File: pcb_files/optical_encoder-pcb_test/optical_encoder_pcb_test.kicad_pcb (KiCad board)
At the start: 2 copper layers, 53.7 x 54.9 mm, 33 parts, among them J1 Conn_01x03_Pin, J2 Conn_01x05_Pin, J3 Conn_01x04_Pin, J4 Conn_01x04_Pin, J5 Conn_DF13_male_01x06, J6 Conn_DF13_male_01x05, J7 Conn_AMASS_male_01x03, J8 Conn_01x03_Pin, U1 AT24CS16-STUM, U2 AMS1117-3.3

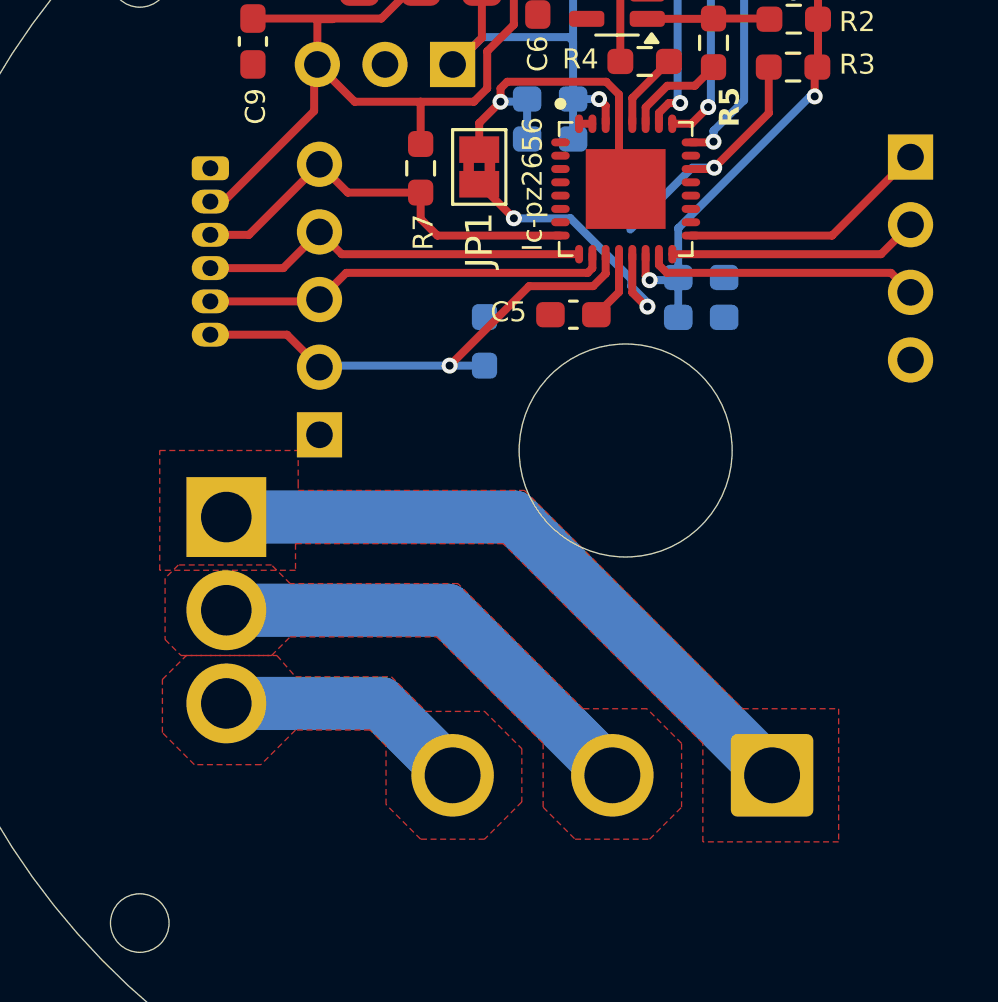
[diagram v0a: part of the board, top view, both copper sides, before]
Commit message: unconnected track removed
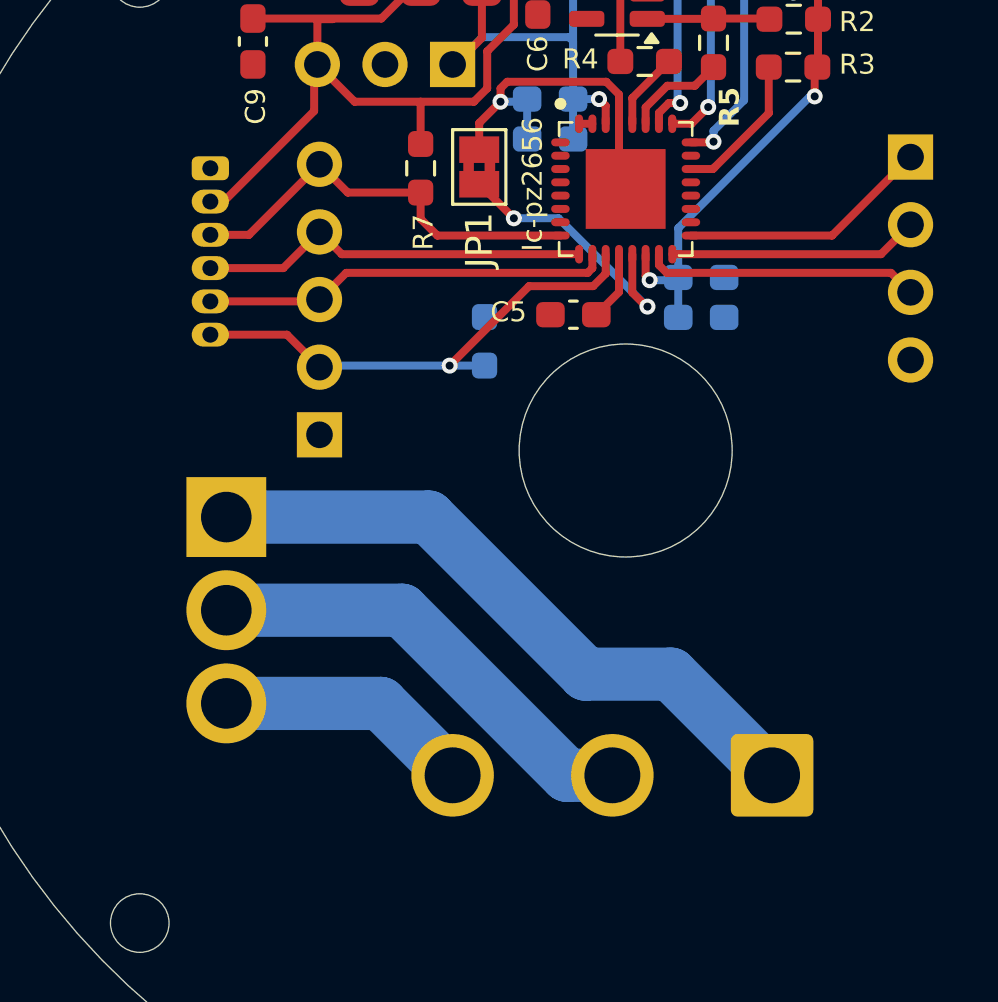
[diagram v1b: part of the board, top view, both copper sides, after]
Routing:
- net Net-(Ic-pz2656-NRES): track 9.64 -> 5.52 mm, vias 1 -> 0
- removed copper zone on F.Cu, net /P1
- removed copper zone on F.Cu, net /P2
- removed copper zone on F.Cu, net /P3
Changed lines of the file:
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@@
 			(pinfunction "Pin_1")
 			(pintype "passive")
+			(zone_connect 2)
+			(thermal_bridge_width 1)
+			(thermal_bridge_angle 45)
+			(thermal_gap 0.5)
 		)
 		(pad "2" thru_hole circle
@@
 	)
 	(gr_text "P1"
-		(at 124.7 133 -0)
+		(at 124.5 132.9 -0)
 		(layer "B.SilkS")
 		(effects
@@
 	)
 	(gr_text "P2"
-		(at 118.7 133 -0)
+		(at 118 134.1 -0)
 		(layer "B.SilkS")
 		(effects
@@
 	)
 	(gr_text "P3"
-		(at 112.7 133 -0)
+		(at 112.9 133.4 -0)
 		(layer "B.SilkS")
 		(effects
@@
 	)
 	(segment
-		(start 121.318804 116.941889)
+		(start 116.3 113.7775)
+		(end 117.9775 113.7775)
+		(width 0.3)
+		(layer "B.Cu")
+		(net 3)
+	)
+	(segment
+		(start 121.295871 117.095871)
 		(end 121.318804 117.095871)
 		(width 0.3)
@@
 	)
 	(segment
-		(start 120.713173 116.336258)
-		(end 121.318804 116.941889)
-		(width 0.3)
-		(layer "B.Cu")
-		(net 3)
-	)
-	(segment
-		(start 116.3 113.7775)
-		(end 118.427502 113.7775)
-		(width 0.3)
-		(layer "B.Cu")
-		(net 3)
-	)
-	(segment
-		(start 120.713173 116.063171)
-		(end 120.713173 116.336258)
-		(width 0.3)
-		(layer "B.Cu")
-		(net 3)
-	)
-	(segment
-		(start 118.427502 113.7775)
-		(end 120.713173 116.063171)
+		(start 117.9775 113.7775)
+		(end 121.295871 117.095871)
 		(width 0.3)
 		(layer "B.Cu")
@@
 		(net 17)
 	)
-	(via
-		(at 123.82644 111.87932)
-		(size 0.6)
-		(drill 0.3)
-		(layers "F.Cu" "B.Cu")
-		(net 17)
-	)
-	(segment
-		(start 122.99568 111.87932)
-		(end 120.675 114.2)
-		(width 0.3)
-		(layer "B.Cu")
-		(net 17)
-	)
-	(segment
-		(start 123.82644 111.87932)
-		(end 122.99568 111.87932)
-		(width 0.3)
-		(layer "B.Cu")
-		(net 17)
-	)
 	(segment
 		(start 107.64 115.65)
@@
 	)
 	(segment
-		(start 116.3 125)
+		(start 113.1 125)
+		(end 119 130.9)
+		(width 2)
+		(layer "B.Cu")
+		(net 32)
+	)
+	(segment
+		(start 119 130.9)
+		(end 122.2 130.9)
+		(width 2)
+		(layer "B.Cu")
+		(net 32)
+	)
+	(segment
+		(start 122.2 130.9)
 		(end 126 134.7)
 		(width 2)
@@
 	(segment
 		(start 105.5 125)
-		(end 116.3 125)
+		(end 113.1 125)
 		(width 2)
 		(layer "B.Cu")
@@
 	(segment
 		(start 105.5 128.5)
-		(end 113.8 128.5)
+		(end 112.1 128.5)
 		(width 2)
 		(layer "B.Cu")
@@
 	)
 	(segment
-		(start 113.8 128.5)
+		(start 112.1 128.5)
+		(end 118.3 134.7)
+		(width 2)
+		(layer "B.Cu")
+		(net 33)
+	)
+	(segment
+		(start 118.3 134.7)
 		(end 120 134.7)
 		(width 2)
@@
 	)
 	(zone
-		(net 31)
-		(net_name "/P3")
-		(layer "F.Cu")
-		(hatch edge 0.5)
-		(priority 1)
-		(connect_pads
-			(clearance 0)
-		)
-		(min_thickness 0.25)
-		(filled_areas_thickness no)
-		(fill yes
-			(thermal_gap 0.5)
-			(thermal_bridge_width 0.5)
-		)
-		(polygon
-			(pts
-				(xy 103.1 131.1) (xy 104 130.2) (xy 107.4 130.2) (xy 108.1 131) (xy 111.7 131) (xy 113 132.3) (xy 115.2 132.3)
-				(xy 116.6 133.7) (xy 116.6 135.7) (xy 115.2 137.1) (xy 112.8 137.1) (xy 111.5 135.8) (xy 111.5 133.6)
-				(xy 110.9 133) (xy 108.1 133) (xy 106.8 134.3) (xy 104.3 134.3) (xy 103.1 133.1)
-			)
-		)
-	)
-	(zone
-		(net 33)
-		(net_name "/P2")
-		(layer "F.Cu")
-		(hatch edge 0.5)
-		(priority 3)
-		(connect_pads
-			(clearance 0)
-		)
-		(min_thickness 0.25)
-		(filled_areas_thickness no)
-		(fill yes
-			(thermal_gap 0.5)
-			(thermal_bridge_width 0.5)
-		)
-		(polygon
-			(pts
-				(xy 118.6 137.1) (xy 121.4 137.1) (xy 122.6 135.9) (xy 122.6 133.5) (xy 121.3 132.2) (xy 118.9 132.2)
-				(xy 114.2 127.5) (xy 107.9 127.5) (xy 107.2 126.8) (xy 103.7 126.8) (xy 103.2 127.3) (xy 103.2 129.6)
-				(xy 103.8 130.2) (xy 107.2 130.2) (xy 107.9 129.5) (xy 113.4 129.5) (xy 117.4 133.5) (xy 117.4 135.9)
-			)
-		)
-	)
-	(zone
-		(net 32)
-		(net_name "/P1")
-		(layer "F.Cu")
-		(hatch edge 0.5)
-		(priority 2)
-		(connect_pads
-			(clearance 0)
-		)
-		(min_thickness 0.25)
-		(filled_areas_thickness no)
-		(fill yes
-			(thermal_gap 0.5)
-			(thermal_bridge_width 0.5)
-		)
-		(polygon
-			(pts
-				(xy 103 122.5) (xy 108.2 122.5) (xy 108.2 123.7) (xy 108.2 124) (xy 116.7 124) (xy 124.9 132.2)
-				(xy 128.5 132.2) (xy 128.5 137.2) (xy 123.4 137.2) (xy 123.4 133.5) (xy 115.9 126) (xy 108.1 126)
-				(xy 108.1 127) (xy 103 127)
-			)
-		)
-	)
-	(zone

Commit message: connexion issues fixed, ibon file added
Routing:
- net GND: track 10.8 -> 13.3 mm, vias 3 -> 4

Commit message: mounting holes replaced
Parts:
- moved REF** 0.36 mm to (138.5, 104.5)
- moved REF** 0.36 mm to (102.5, 140.5)
- moved REF** 0.36 mm to (102.5, 104.5)
- moved REF** 0.36 mm to (138.5, 140.5)
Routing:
- net (no net): vias 0 -> 1
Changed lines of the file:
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@@
 		(pad_to_mask_clearance 0)
 		(allow_soldermask_bridges_in_footprints no)
+		(aux_axis_origin 120.5 122.5)
+		(grid_origin 120.5 122.5)
 		(pcbplotparams
 			(layerselection 0x00010fc_ffffffff)
@@
 	(footprint "MountingHole:MountingHole_2.2mm_M2"
 		(layer "B.Cu")
-		(at 138.75 104.75 180)
+		(at 138.53 104.47 180)
 		(descr "Mounting Hole 2.2mm, no annular, M2")
 		(tags "mounting hole 2.2mm no annular m2")
@@
 	(footprint "MountingHole:MountingHole_2.2mm_M2"
 		(layer "B.Cu")
-		(at 102.25 140.25 180)
+		(at 102.47 140.53 180)
 		(descr "Mounting Hole 2.2mm, no annular, M2")
 		(tags "mounting hole 2.2mm no annular m2")
@@
 	(footprint "MountingHole:MountingHole_2.2mm_M2"
 		(layer "B.Cu")
-		(at 102.25 104.75 180)
+		(at 102.47 104.47 180)
 		(descr "Mounting Hole 2.2mm, no annular, M2")
 		(tags "mounting hole 2.2mm no annular m2")
@@
 	(footprint "MountingHole:MountingHole_2.2mm_M2"
 		(layer "B.Cu")
-		(at 138.75 140.25 180)
+		(at 138.53 140.53 180)
 		(descr "Mounting Hole 2.2mm, no annular, M2")
 		(tags "mounting hole 2.2mm no annular m2")
@@
 	)
 	(gr_line
-		(start 138.75 140.25)
-		(end 138.75 104.75)
-		(stroke
-			(width 0.2)
-			(type default)
-		)
-		(layer "Dwgs.User")
-	)
-	(gr_line
 		(start 120.5 122.5)
 		(end 120.5 112.55)
@@
 	)
 	(gr_line
-		(start 102.25 140.25)
-		(end 138.75 140.25)
-		(stroke
-			(width 0.2)
-			(type default)
-		)
-		(layer "Dwgs.User")
-	)
-	(gr_circle
-		(center 120.5 122.5)
-		(end 146 122.5)
-		(stroke
-			(width 0.2)
-			(type default)
-		)
-		(fill none)
-		(layer "Dwgs.User")
-	)
-	(gr_line
-		(start 102.25 140.25)
-		(end 102.25 104.75)
-		(stroke
-			(width 0.2)
-			(type default)
-		)
-		(layer "Dwgs.User")
-	)
-	(gr_line
 		(start 94.25 108.75)
 		(end 94.25 136.25)
@@
 		)
 	)
+	(dimension
+		(type aligned)
+		(layer "Dwgs.User")
+		(pts
+			(xy 102.47 140.53) (xy 138.53 140.53)
+		)
+		(height 14.969999)
+		(gr_text "36,0600 mm"
+			(at 120.5 154.349999 0)
+			(layer "Dwgs.User")
+			(effects
+				(font
+					(size 1 1)
+					(thickness 0.15)
+				)
+			)
+		)
+		(format
+			(prefix "")
+			(suffix "")
+			(units 3)
+			(units_format 1)
+			(precision 4)
+		)
+		(style
+			(thickness 0.1)
+			(arrow_length 1.27)
+			(text_position_mode 0)
+			(extension_height 0.58642)
+			(extension_offset 0.5) keep_text_aligned)
+	)
+	(dimension
+		(type aligned)
+		(layer "Dwgs.User")
+		(pts
+			(xy 120.5 122.5) (xy 102.47 140.53)
+		)
+		(height -45.957857)
+		(gr_text "25,4983 mm"
+			(at 143.168939 163.198939 45)
+			(layer "Dwgs.User")
+			(effects
+				(font
+					(size 1 1)
+					(thickness 0.15)
+				)
+			)
+		)
+		(format
+			(prefix "")
+			(suffix "")
+			(units 3)
+			(units_format 1)
+			(precision 4)
+		)
+		(style
+			(thickness 0.1)
+			(arrow_length 1.27)
+			(text_position_mode 0)
+			(extension_height 0.58642)
+			(extension_offset 0.5) keep_text_aligned)
+	)
+	(dimension
+		(type aligned)
+		(layer "Dwgs.User")
+		(pts
+			(xy 138.53 140.53) (xy 138.53 104.47)
+		)
+		(height 16.17)
+		(gr_text "36,0600 mm"
+			(at 153.55 122.5 90)
+			(layer "Dwgs.User")
+			(effects
+				(font
+					(size 1 1)
+					(thickness 0.15)
+				)
+			)
+		)
+		(format
+			(prefix "")
+			(suffix "")
+			(units 3)
+			(units_format 1)
+			(precision 4)
+		)
+		(style
+			(thickness 0.1)
+			(arrow_length 1.27)
+			(text_position_mode 0)
+			(extension_height 0.58642)
+			(extension_offset 0.5) keep_text_aligned)
+	)
+	(via
+		(at 120.5 122.5)
+		(size 0.6)
+		(drill 0.3)
+		(layers "F.Cu" "B.Cu")
+		(net 0)
+	)
 	(segment
